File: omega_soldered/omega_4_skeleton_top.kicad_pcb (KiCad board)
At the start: 2 copper layers, 204.8 x 88 mm, 1 part

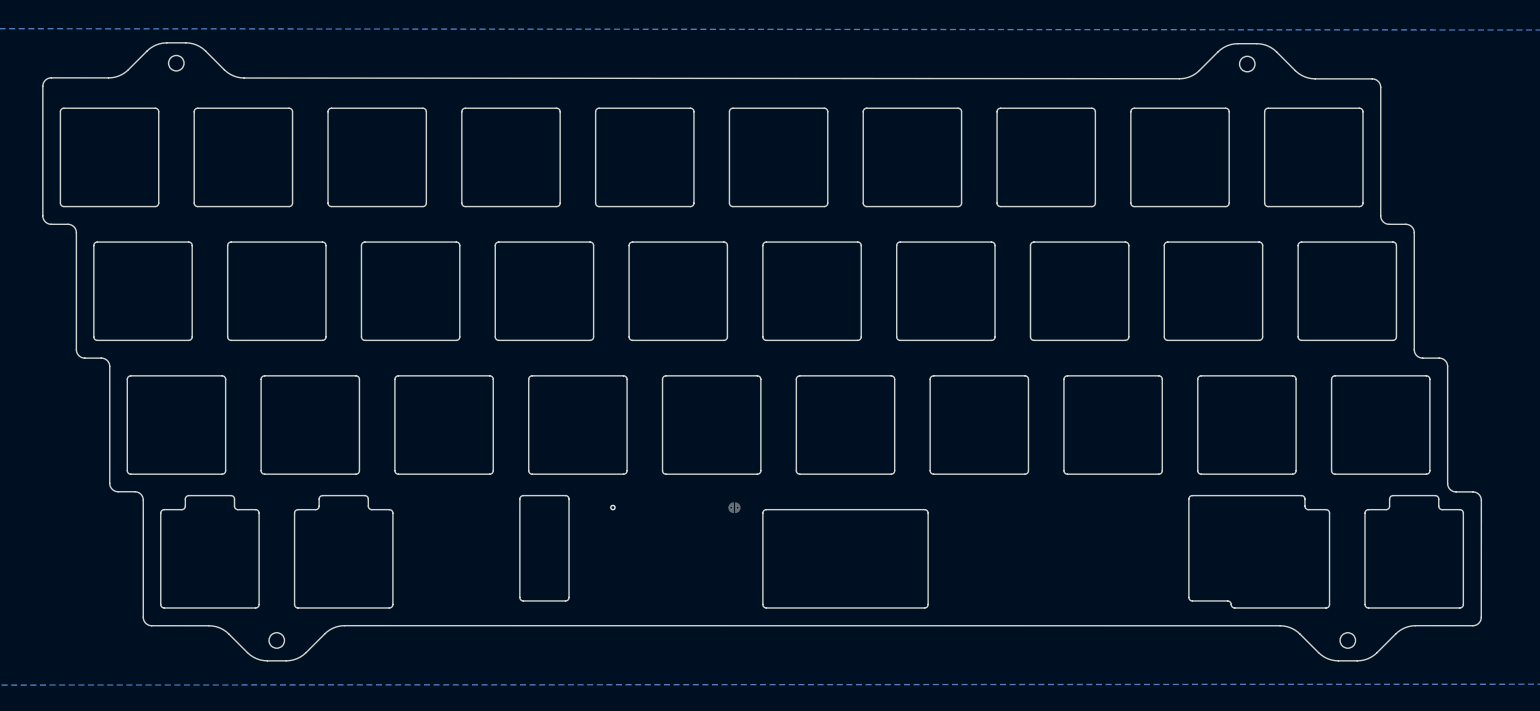
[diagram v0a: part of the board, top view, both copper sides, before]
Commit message: update skeleton case to allow 3mm between cuts and regen prod files
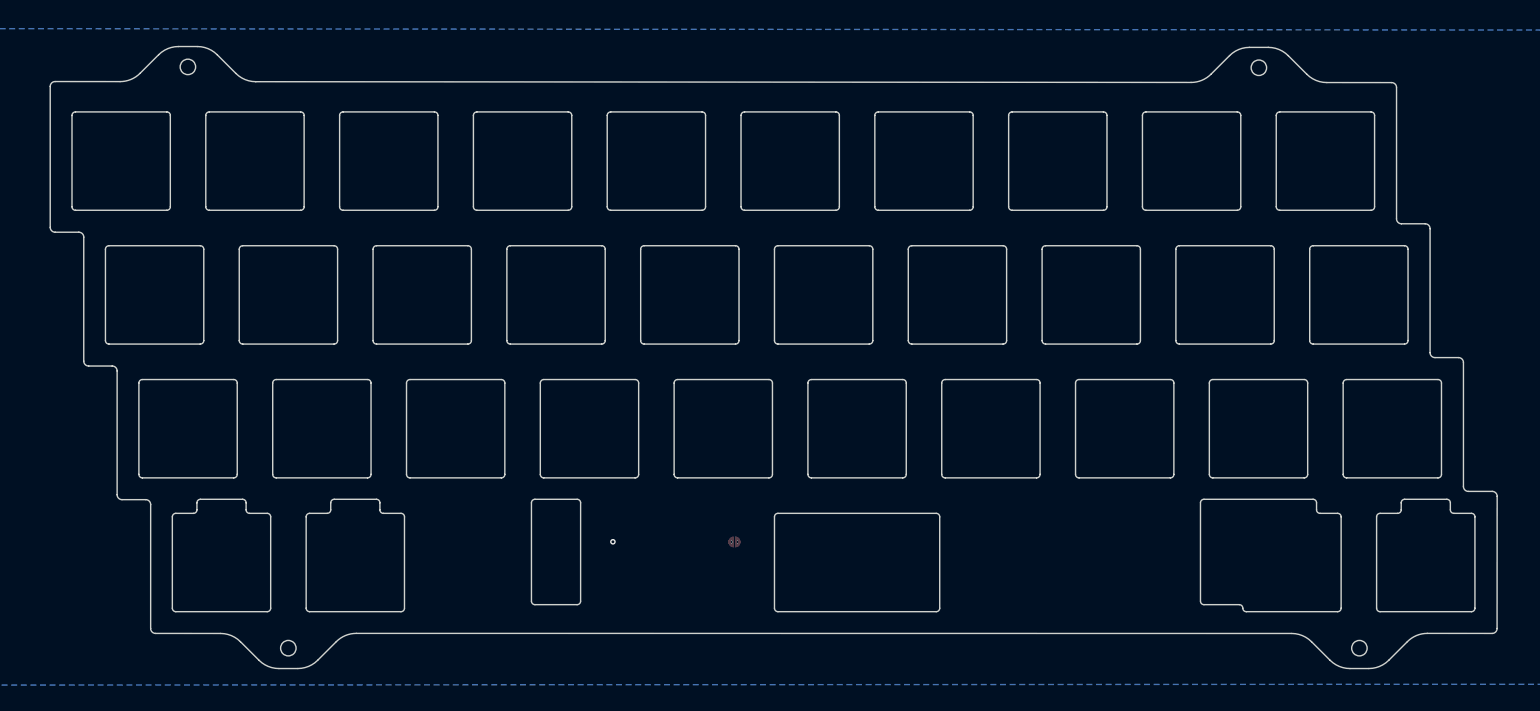
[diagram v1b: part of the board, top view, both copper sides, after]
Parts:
- moved JP1 4.88 mm to (142.8, 117.8)
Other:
- board size 204.8 x 88 mm -> 206 x 88.6 mm

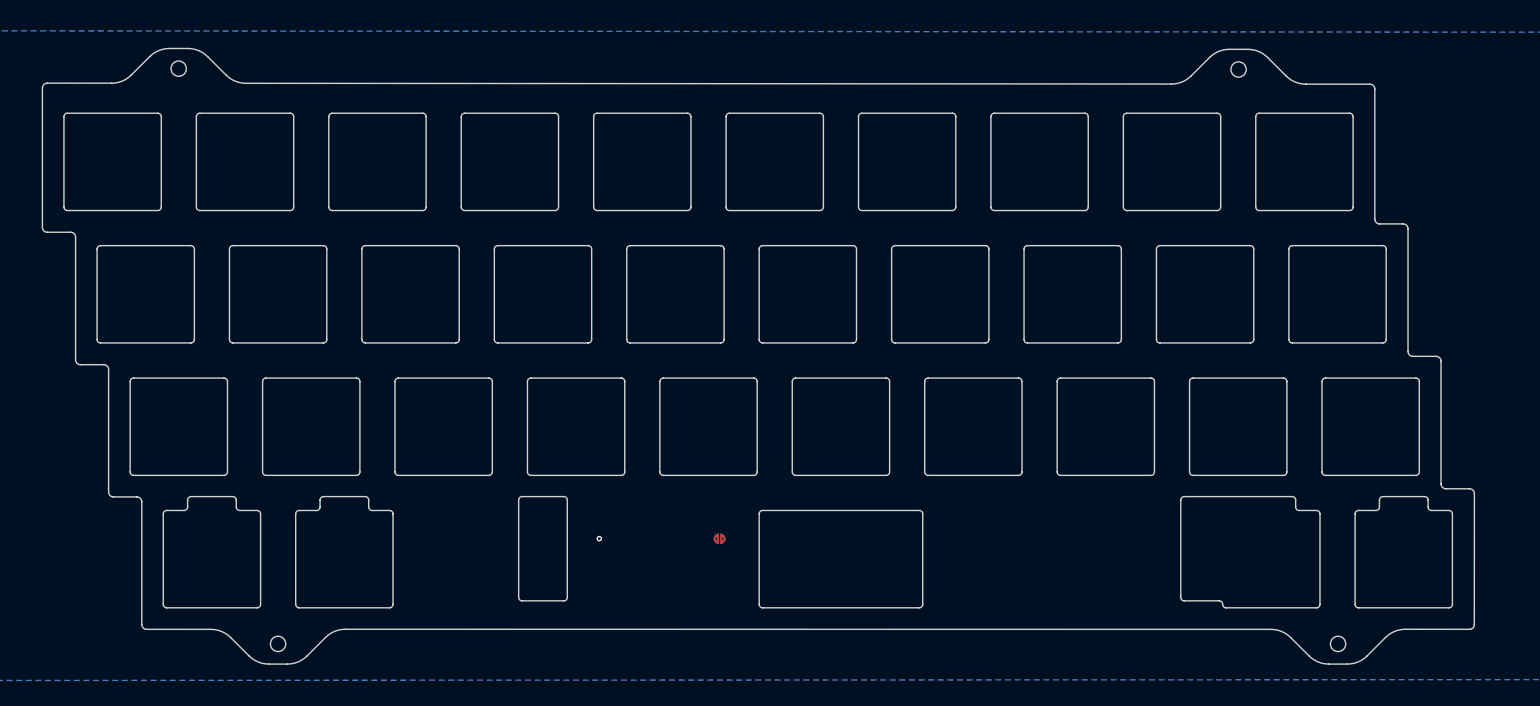
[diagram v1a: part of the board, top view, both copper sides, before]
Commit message: update omega4 case files
move stabilizer cutouts
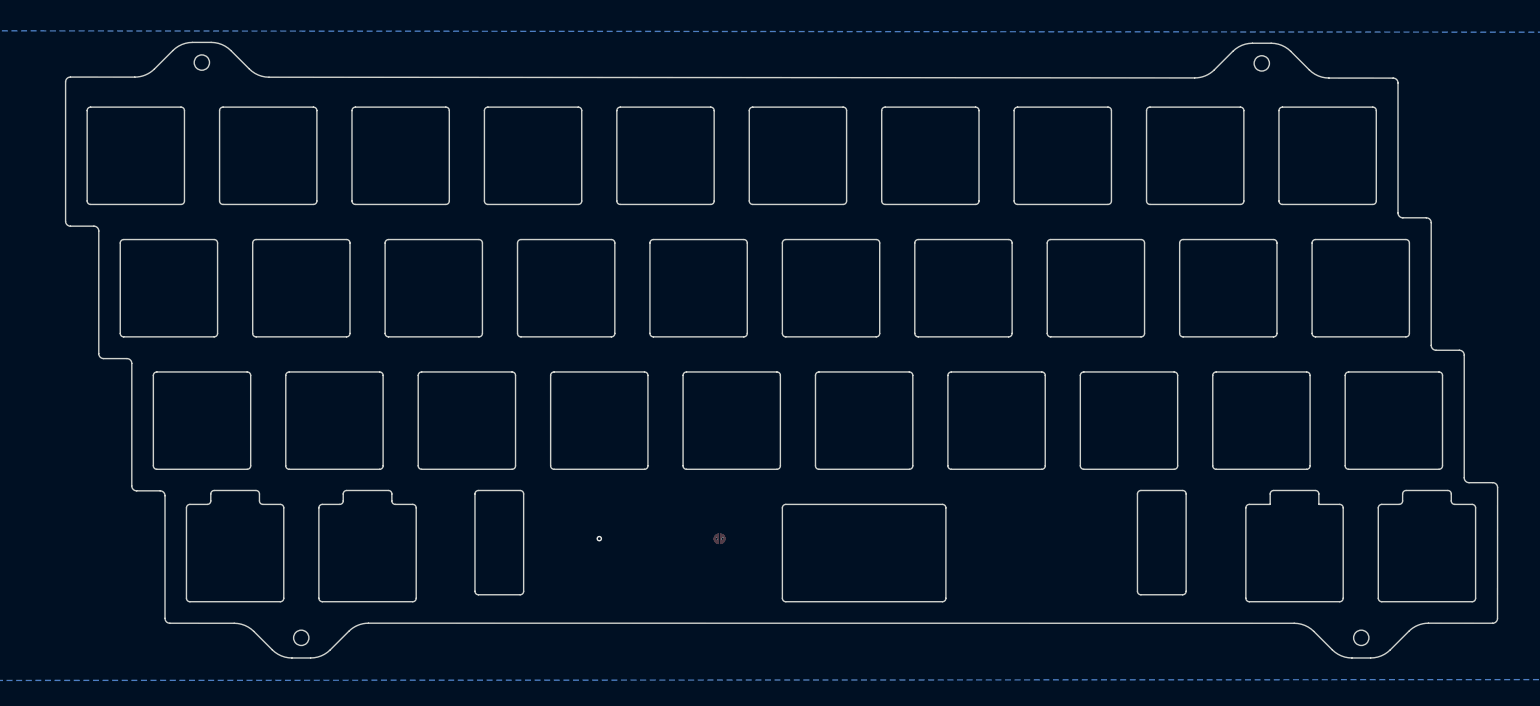
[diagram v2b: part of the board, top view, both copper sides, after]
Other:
- outline, holes or cut-outs redrawn
